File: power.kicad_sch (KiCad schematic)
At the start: 22 parts, among them U3 MCP1700x-330xxTT

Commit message: Finished system overview
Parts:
- removed JP2: SolderJumper_2_Bridged, Jumper:SolderJumper-2_P1.3mm_Bridged2Bar_Pad1.0x1.5mm, symbol Jumper:SolderJumper_2_Bridged
- added JP4: SolderJumper_2_Bridged, Jumper:SolderJumper-2_P1.3mm_Bridged2Bar_Pad1.0x1.5mm, symbol Jumper:SolderJumper_2_Bridged
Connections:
- net +9V: no longer C11.1, C18.1, PS1.6 (VIN)
- net DGND: now also JP4.2 (B); no longer C1.2
- net PGND: now also C1.2, JP4.1 (A)
- new net +VBAT: C11.1, C18.1, PS1.6 (VIN)
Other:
- note added: "10-25.2V @ (0, 3, 100)A"
- note added: "5V @ (0, 500, 3000)mA"
- note added: "Battery Voltage: 4S-6S (10-26VDC)"
- note added: "Buck Converter 10-26V to 9V 2A"
- note added: "DESIGN NOTE: JP4 is the Power Ground (PGND) to Digital Ground (DGND) connection."
- note added: "LDO 3V3 @ (0, 50, 200)mA"
- note removed: "10-26V"
- note removed: "10-26V to 9V 2A Step-down converter."
- note removed: "2000mA"
- note removed: "3V3 @ (0, 50, 200)mA"
- note removed: "5V @ (0, 60, 500)mA"

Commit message: First schematic draft complete
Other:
- note added: "DESIGN NOTE: R_FBT = ( (V_OUT - V_REF) / V_REF) * R_FBB R_FBT = ( (9V - 0.6V) / 0.6V) * 10k R_FBT = 140k V_OUT = 9V, V_REF = 0.6V, R11 = 10k, R6 = 140k"
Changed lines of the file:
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@@
+		)
+	)
+	(text "DESIGN NOTE:\nR_FBT = ( (V_OUT - V_REF) / V_REF) * R_FBB\nR_FBT = ( (9V - 0.6V) / 0.6V) * 10k\nR_FBT = 140k\n\nV_OUT = 9V, V_REF = 0.6V, R11 = 10k, R6 = 140k"
+		(exclude_from_sim no)
+		(at 148.336 89.408 0)
+		(effects
+			(font
+				(size 1.27 1.27)
+			)
+			(justify left)
 		)
 	)
@@
 	(text "FB = 9V OUT"
 		(exclude_from_sim no)
-		(at 173.482 56.896 0)
+		(at 172.974 60.706 0)
 		(effects
 			(font

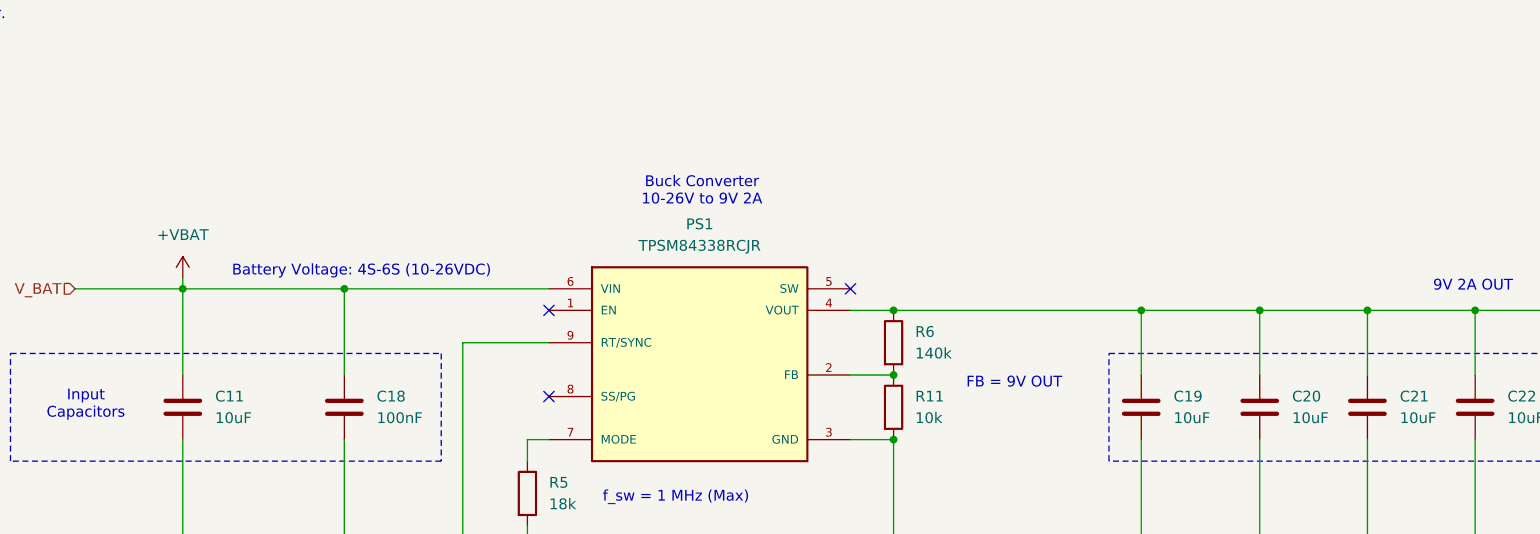
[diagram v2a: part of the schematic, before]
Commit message: Wiring Complete, ERC and DRC remaining
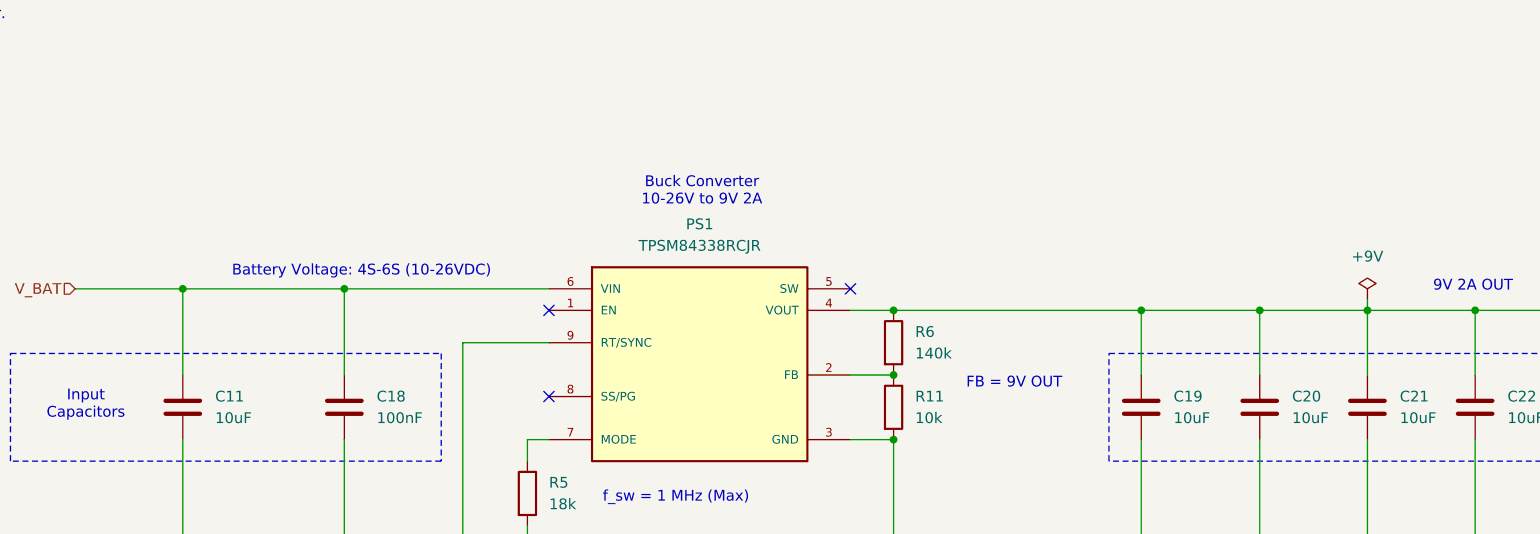
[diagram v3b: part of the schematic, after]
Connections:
- net +VBAT renamed V_BAT
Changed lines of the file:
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@@
 	)
 	(junction
-		(at 74.93 49.53)
-		(diameter 0)
-		(color 0 0 0 0)
-	)
-	(junction
 		(at 93.98 49.53)
 		(diameter 0)
@@
 	)
 	(junction
+		(at 74.93 49.53)
+		(diameter 0)
+		(color 0 0 0 0)
+	)
+	(junction
 		(at 158.75 59.69)
 		(diameter 0)
@@
 	(wire
 		(pts
-			(xy 74.93 49.53) (xy 93.98 49.53)
+			(xy 62.23 49.53) (xy 74.93 49.53)
 		)
 		(stroke
@@
 	(wire
 		(pts
-			(xy 133.35 133.35) (xy 137.16 133.35)
+			(xy 214.63 50.8) (xy 214.63 52.07)
 		)
 		(stroke
@@
 	(wire
 		(pts
-			(xy 151.13 120.65) (xy 151.13 123.19)
+			(xy 133.35 133.35) (xy 137.16 133.35)
 		)
 		(stroke
@@
 	(wire
 		(pts
-			(xy 31.75 175.26) (xy 31.75 180.34)
+			(xy 151.13 120.65) (xy 151.13 123.19)
 		)
 		(stroke
@@
 	(wire
 		(pts
-			(xy 60.96 80.01) (xy 74.93 80.01)
+			(xy 31.75 175.26) (xy 31.75 180.34)
 		)
 		(stroke
@@
 	(wire
 		(pts
-			(xy 187.96 52.07) (xy 201.93 52.07)
+			(xy 60.96 80.01) (xy 74.93 80.01)
 		)
 		(stroke
@@
 	(wire
 		(pts
-			(xy 62.23 49.53) (xy 74.93 49.53)
+			(xy 187.96 52.07) (xy 201.93 52.07)
 		)
 		(stroke
@@
 	(wire
 		(pts
+			(xy 74.93 49.53) (xy 93.98 49.53)
+		)
+		(stroke
+			(width 0)
+			(type default)
+		)
+	)
+	(wire
+		(pts
 			(xy 137.16 128.27) (xy 137.16 133.35)
 		)
@@
 	(wire
 		(pts
+			(xy 74.93 49.53) (xy 74.93 59.69)
+		)
+		(stroke
+			(width 0)
+			(type default)
+		)
+	)
+	(wire
+		(pts
 			(xy 227.33 52.07) (xy 227.33 59.69)
 		)
@@
 	(wire
 		(pts
-			(xy 74.93 49.53) (xy 74.93 59.69)
-		)
-		(stroke
-			(width 0)
-			(type default)
-		)
-	)
-	(wire
-		(pts
 			(xy 97.79 123.19) (xy 104.14 123.19)
 		)
@@
 	(wire
 		(pts
-			(xy 74.93 48.26) (xy 74.93 49.53)
-		)
-		(stroke
-			(width 0)
-			(type default)
-		)
-	)
-	(wire
-		(pts
 			(xy 74.93 80.01) (xy 74.93 67.31)
 		)
@@
 	)
 	(symbol
+		(lib_id "power:PWR_FLAG")
+		(at 214.63 50.8 0)
+		(unit 1)
+		(exclude_from_sim no)
+		(in_bom yes)
+		(on_board yes)
+		(dnp no)
+		(fields_autoplaced yes)
+		(property "Reference" "#FLG02"
+			(at 214.63 48.895 0)
+			(effects
+				(font
+					(size 1.27 1.27)
+				)
+				(hide yes)
+			)
+		)
+		(property "Value" "+9V"
+			(at 214.63 45.72 0)
+			(effects
+				(font
+					(size 1.27 1.27)
+				)
+			)
+		)
+		(property "Footprint" ""
+			(at 214.63 50.8 0)
+			(effects
+				(font
+					(size 1.27 1.27)
+				)
+				(hide yes)
+			)
+		)
+		(property "Datasheet" "~"
+			(at 214.63 50.8 0)
+			(effects
+				(font
+					(size 1.27 1.27)
+				)
+				(hide yes)
+			)
+		)
+		(property "Description" "Special symbol for telling ERC where power comes from"
+			(at 214.63 50.8 0)
+			(effects
+				(font
+					(size 1.27 1.27)
+				)
+				(hide yes)
+			)
+		)
+		(pin "1"
+		)
+		(instances
+			(project ""
+				(path "/f9e05184-c88b-4a88-ae9c-ab2bdb32be7c/c5103ceb-5325-4a84-a025-9638a412984e/253d5c3b-3006-4c7f-964a-fd84ac77ef63"
+					(reference "#FLG02")
+					(unit 1)
+				)
+			)
+		)
+	)
+	(symbol
 		(lib_id "power:GND1")
 		(at 78.74 180.34 0)
@@
 					(unit 1)
 				)
-			)
-		)
-	)
-	(symbol
-		(lib_id "power:+1V5")
-		(at 74.93 48.26 0)
-		(unit 1)
-		(exclude_from_sim no)
-		(in_bom yes)
-		(on_board yes)
-		(dnp no)
-		(property "Reference" "#PWR033"
-			(at 74.93 52.07 0)
-			(effects
-				(font
-					(size 1.27 1.27)
-				)
-				(hide yes)
-			)
-		)
-		(property "Value" "+VBAT"
-			(at 74.93 43.18 0)
-			(effects
-				(font
-					(size 1.27 1.27)
-				)
-			)
-		)
-		(property "Footprint" ""
-			(at 74.93 48.26 0)
-			(effects
-				(font
-					(size 1.27 1.27)
-				)
-				(hide yes)
-			)
-		)
-		(property "Datasheet" ""
-			(at 74.93 48.26 0)
-			(effects
-				(font
-					(size 1.27 1.27)
-				)
-				(hide yes)
-			)
-		)
-		(property "Description" "Power symbol creates a global label with name \"+1V5\""
-			(at 74.93 48.26 0)
-			(effects
-				(font
-					(size 1.27 1.27)
-				)
-				(hide yes)
-			)
-		)
-		(pin "1"
-		)
-		(instances
-			(project "FCU3"
-				(path "/f9e05184-c88b-4a88-ae9c-ab2bdb32be7c/c5103ceb-5325-4a84-a025-9638a412984e/253d5c3b-3006-4c7f-964a-fd84ac77ef63"
-					(reference "#PWR033")
-					(unit 1)
-				)

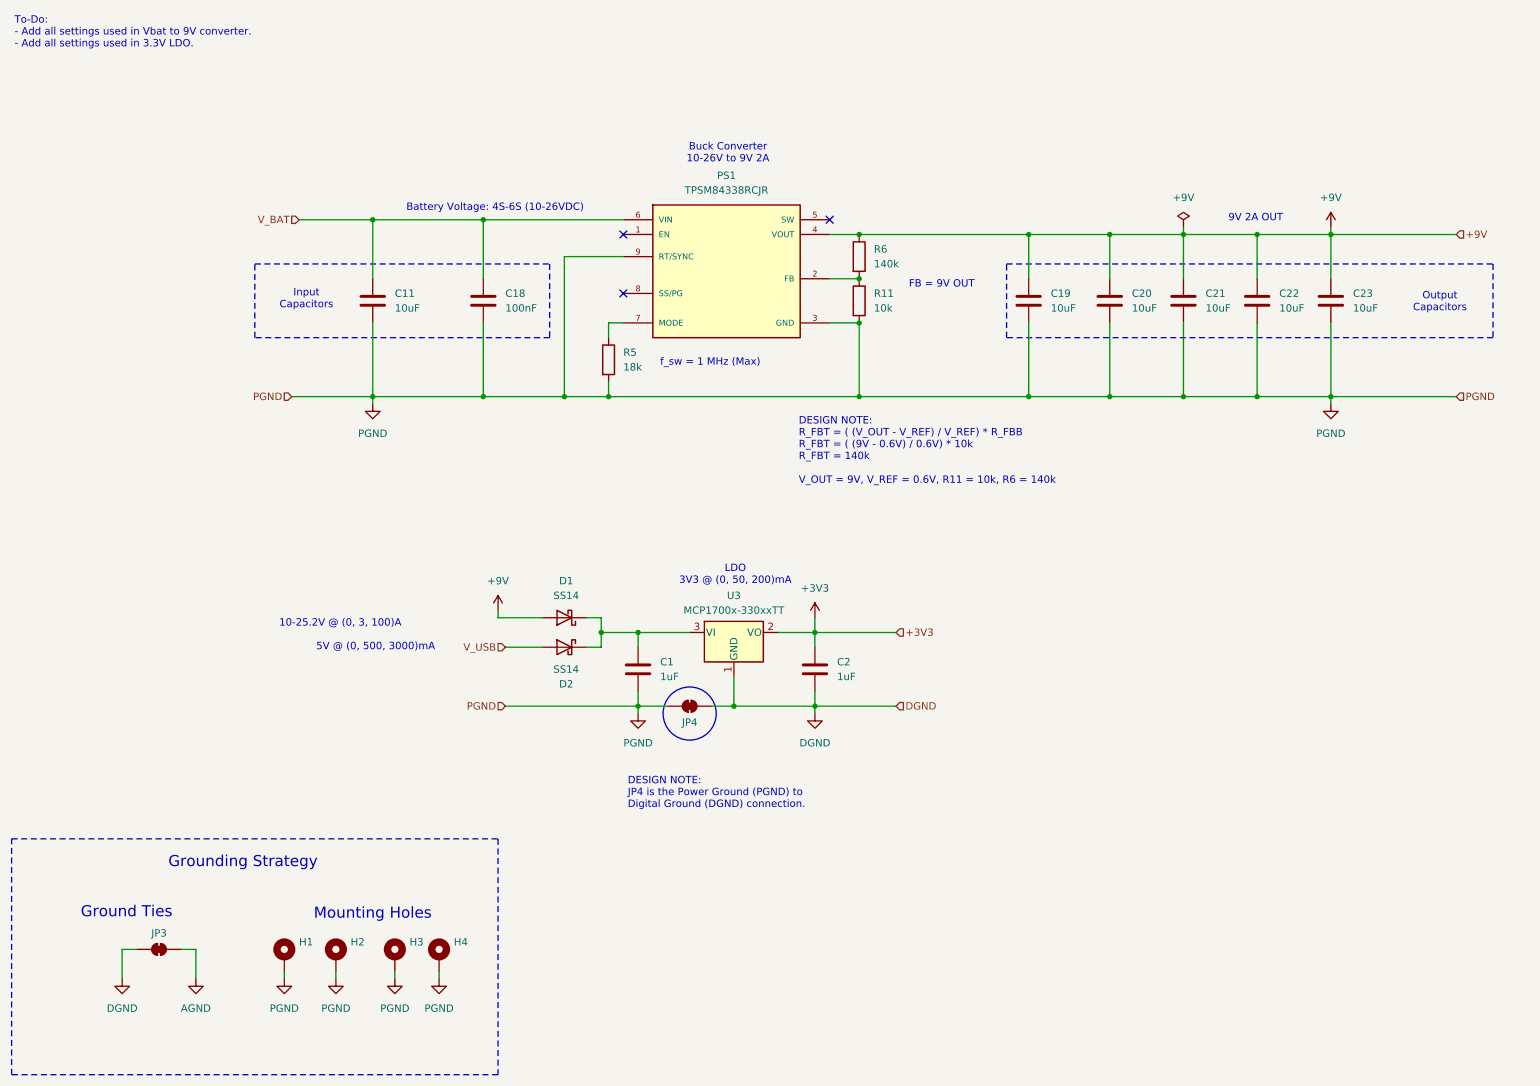
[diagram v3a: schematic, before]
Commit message: Modularized BEC and fixed generic components in schematic.
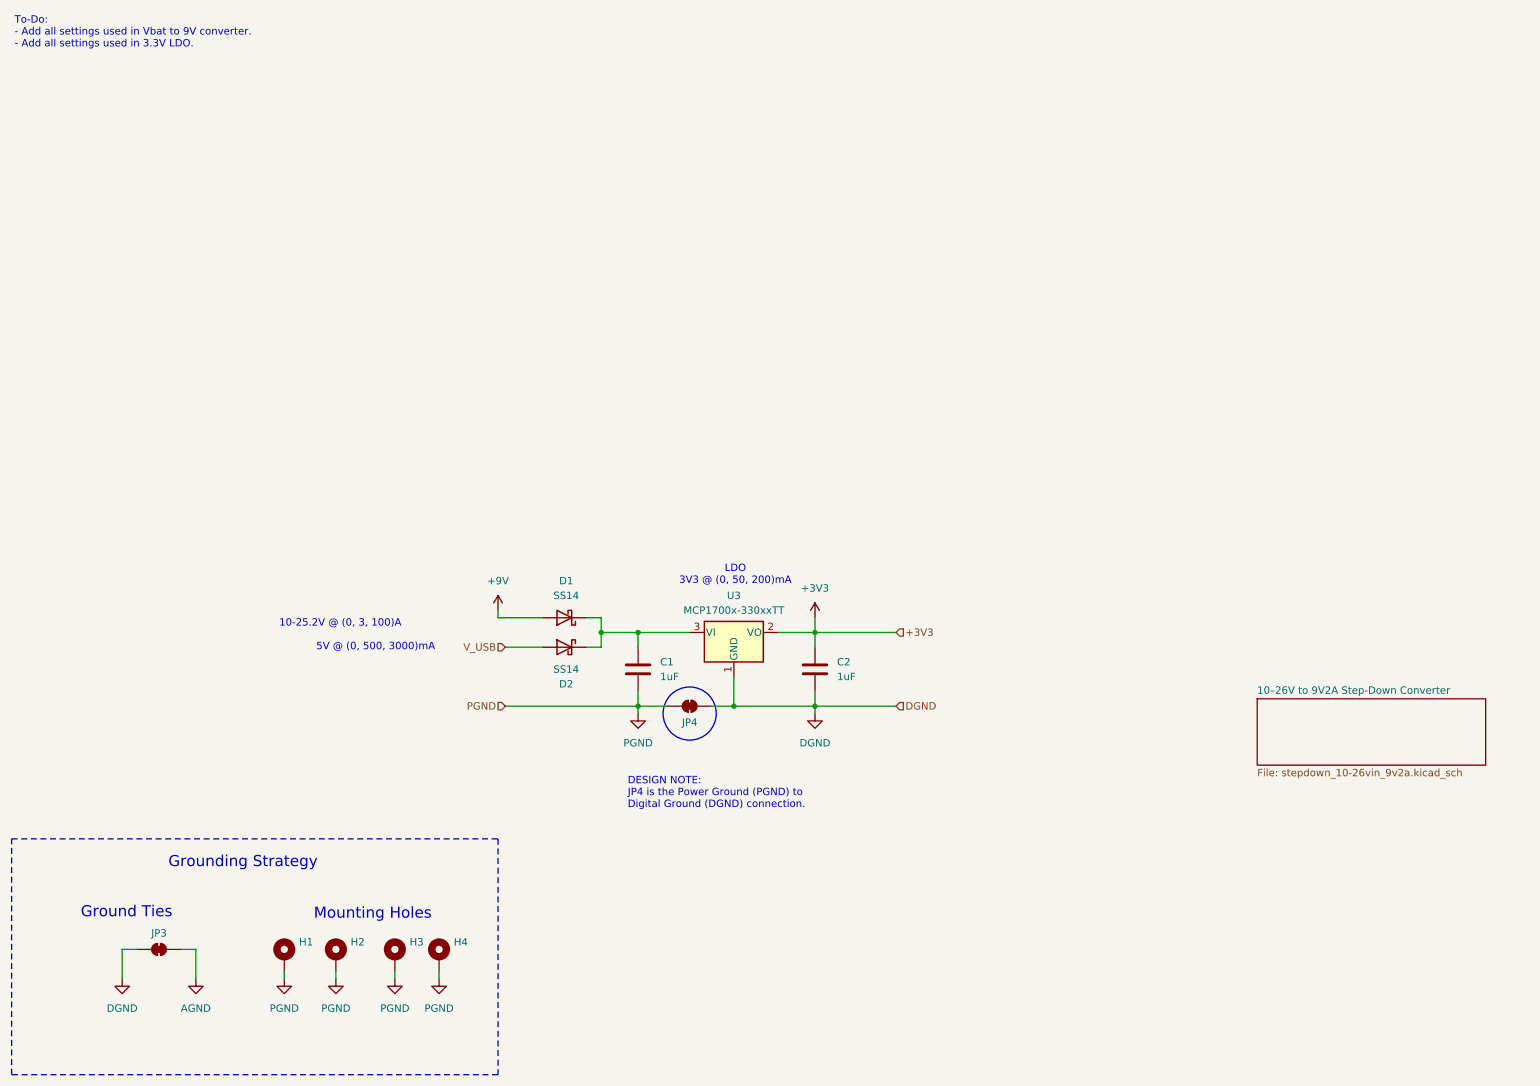
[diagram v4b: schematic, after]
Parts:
- removed C11: 10uF, Capacitor_SMD:C_0603_1608Metric_Pad1.08x0.95mm_HandSolder, symbol Device:C
- removed C18: 100nF, Capacitor_SMD:C_0603_1608Metric_Pad1.08x0.95mm_HandSolder, symbol Device:C
- removed C19, C20, C21, C22, C23: 10uF, Capacitor_SMD:C_1206_3216Metric, symbol Device:C
- removed PS1: TPSM84338RCJR, KSE_DCDC:TPSM84338RCJR, symbol KSE_DCDC:TPSM84338RCJR
- removed R11: 10k, Resistor_SMD:R_0603_1608Metric_Pad0.98x0.95mm_HandSolder, symbol Device:R
- removed R5: 18k, Resistor_SMD:R_0603_1608Metric_Pad0.98x0.95mm_HandSolder, symbol Device:R
- removed R6: 140k, Resistor_SMD:R_0603_1608Metric_Pad0.98x0.95mm_HandSolder, symbol Device:R
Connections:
- no-connect marks 3 -> 0
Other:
- added sheet 10–26V to 9V2A Step-Down Converter (stepdown_10-26vin_9v2a.kicad_sch)
- note removed: "9V 2A OUT"
- note removed: "Battery Voltage: 4S-6S (10-26VDC)"
- note removed: "Buck Converter 10-26V to 9V 2A"
- note removed: "DESIGN NOTE: R_FBT = ( (V_OUT - V_REF) / V_REF) * R_FBB R_FBT = ( (9V - 0.6V) / 0.6V) * 10k R_FBT = 140k V_OUT = 9V, V_REF = 0.6V, R11 = 10k, R6 = 140k"
- note removed: "FB = 9V OUT"
- note removed: "Input Capacitors"
- note removed: "Output Capacitors"
- note removed: "f_sw = 1 MHz (Max)"

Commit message: Updated LDO with new component standard.
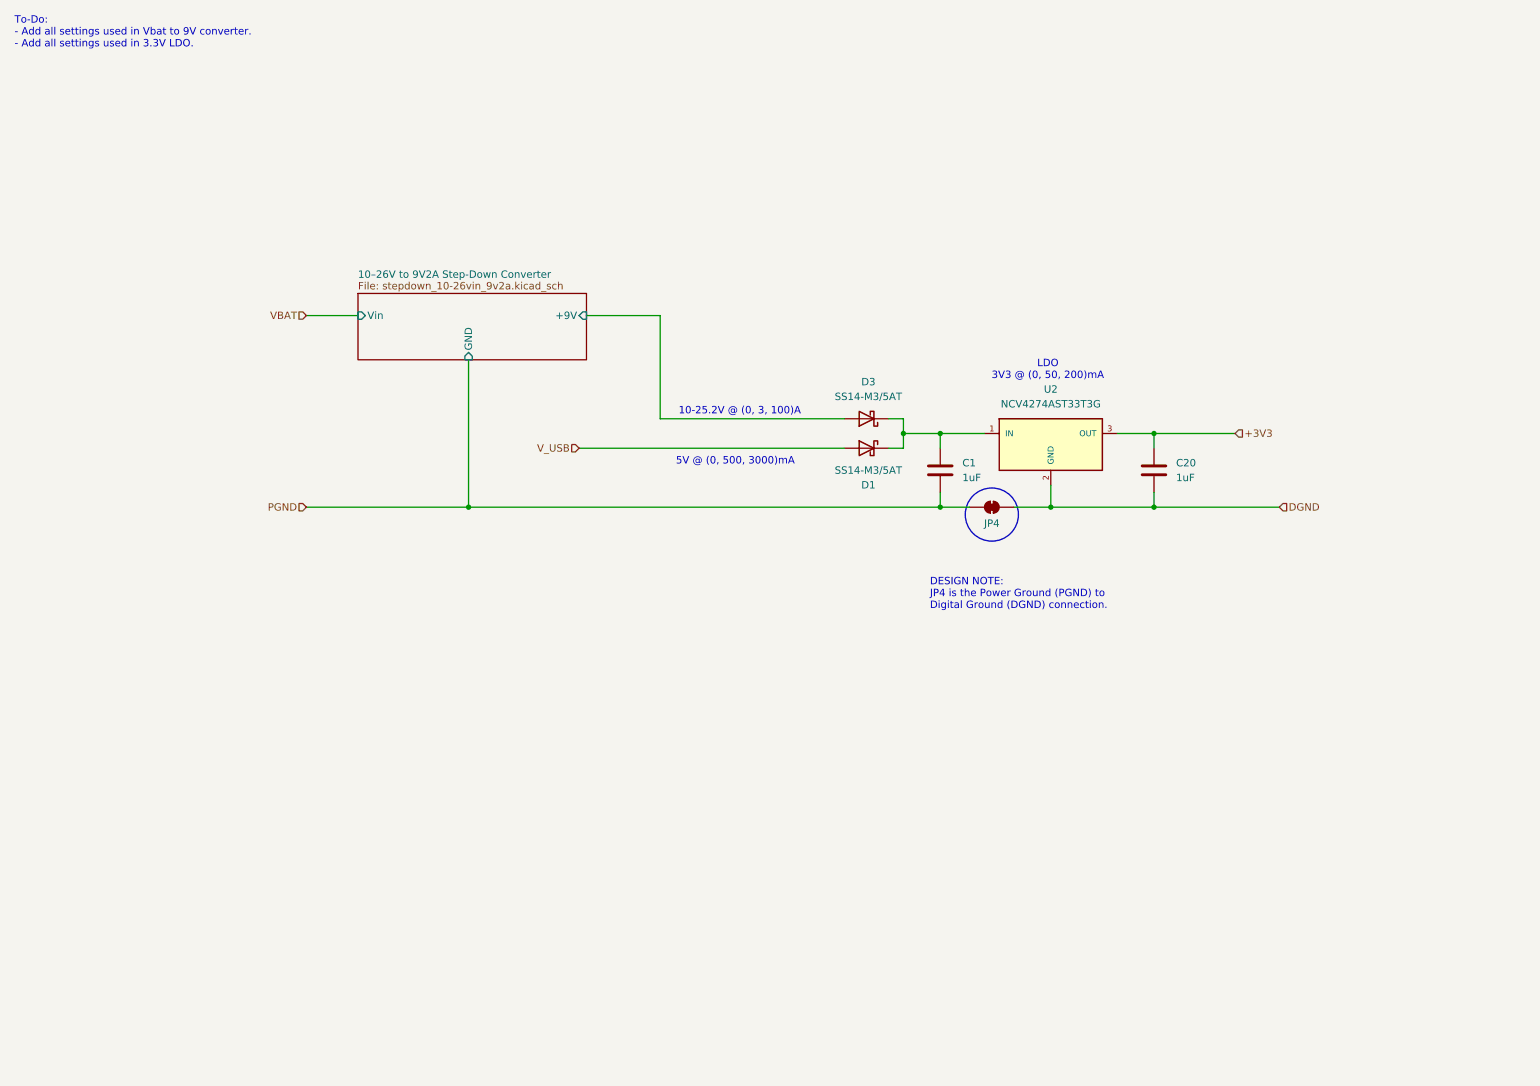
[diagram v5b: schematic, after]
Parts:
- removed C1, C2: 1uF, Capacitor_SMD:C_0603_1608Metric_Pad1.08x0.95mm_HandSolder, symbol Device:C
- removed D1, D2: SS14, Diode_SMD:D_SMA, symbol Diode:SS14
- removed H1, H2, H3, H4: MountingHole_Pad_MP, MountingHole:MountingHole_3.2mm_M3_DIN965_Pad, symbol Mechanical:MountingHole_Pad_MP
- removed JP3: SolderJumper_2_Bridged, Jumper:SolderJumper-2_P1.3mm_Bridged2Bar_Pad1.0x1.5mm, symbol Jumper:SolderJumper_2_Bridged
- removed U3: MCP1700x-330xxTT, Package_TO_SOT_SMD:SOT-23, symbol Regulator_Linear:MCP1700x-330xxTT
- added C1, C20: 1uF, Capacitor_SMD:C_1206_3216Metric, symbol KSE_Capacitors:C
- added D1, D3: SS14-M3/5AT, Diode_SMD:D_SMA, symbol KSE_Diodes:D_Schottky
- added U2: NCV4274AST33T3G, KSE_DCDC:SOT230P700X175-4N, symbol KSE_DCDC:NCV4274AST33T3G
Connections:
- net +3V3: now also C20.1, U2.3 (OUT)
- net PGND: now also C1.2
- net V_USB: now also D1.2 (A)
- net DGND renamed GND
- net GND: now also C20.2, U2.2 (GND), U2.4 (GND)
- new net: C1.1, D1.1 (K), D3.1 (K), U2.1 (IN)
- new net 10–26V to 9V2A Step-Down Converter/+9V: D3.2 (A)
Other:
- sheet 10–26V to 9V2A Step-Down Converter ports: added +9V, GND, Vin; removed none
- note removed: "Ground Ties"
- note removed: "Grounding Strategy"
- note removed: "Mounting Holes"
- moved on the sheet: JP4
